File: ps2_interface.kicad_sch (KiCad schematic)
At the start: 28 parts, among them J1 Mini-DIN-6, J2 Conn_01x13, J3 KBD, U1 74HC595, U2 74HC595, U3 74HC180, U4 74HC08, U5 74HC14

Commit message: Update
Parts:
- removed TP1: REG_CLK, TestPoint:TestPoint_Loop_D2.60mm_Drill1.6mm_Beaded, symbol Connector:TestPoint
- removed TP2: LATCH_CLK, TestPoint:TestPoint_Loop_D2.60mm_Drill1.6mm_Beaded, symbol Connector:TestPoint
- removed U3: 74HC180, Package_DIP:DIP-14_W7.62mm, symbol AK's_Library:74HC180
- added U6: 74HC280, Package_DIP:DIP-14_W7.62mm, symbol 74xx:74LS280
- J2: footprint Connector_PinSocket_2.54mm:PinSocket_1x13_P2.54mm_Vertical -> Connector_PinHeader_2.54mm:PinHeader_1x13_P2.54mm_Vertical
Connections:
- net BUS_ENABLE: now also U5.3; no longer U5.11
- net D0: now also U6.1 (G)
- net D1: now also U6.13 (F)
- net D2: now also U6.8 (A)
- net D3: now also U6.9 (B)
- net D4: now also U6.10 (C)
- net D5: now also U6.11 (D)
- net D6: now also U6.4 (I)
- net D7: now also U6.12 (E)
- net DE: now also U4.12; no longer U4.1
- net DP: now also U6.2 (H); no longer U5.9
- net GND: now also U6.7 (GND)
- net KBD_CLK: now also U5.11; no longer U5.3
- net VALID_PACKET: now also U4.8; no longer U4.6
- net VCC: now also U5.9, U6.14 (VCC); no longer U4.12, U4.9
- net ~{LATCH_CLK}: now also U4.3; no longer U4.8
- net ~{REG_CLK}: now also U4.4, U4.5; no longer U4.13
- net ~{REG_OE}: now also U5.4; no longer U5.10
- net at U4.11: now also U4.9; no longer U4.10
- net at U5.2: now also U4.13; no longer U4.2
- net at D1.2 (A), R1.1: now also U5.10; no longer U5.4
- new net: U4.10, U6.6 (Odd)
- new net: U4.1, U4.2, U4.6
- no-connect marks 9 -> 10
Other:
- moved on the sheet: U4A, U4B, U4C, U4D, U5B, U5D, U5E

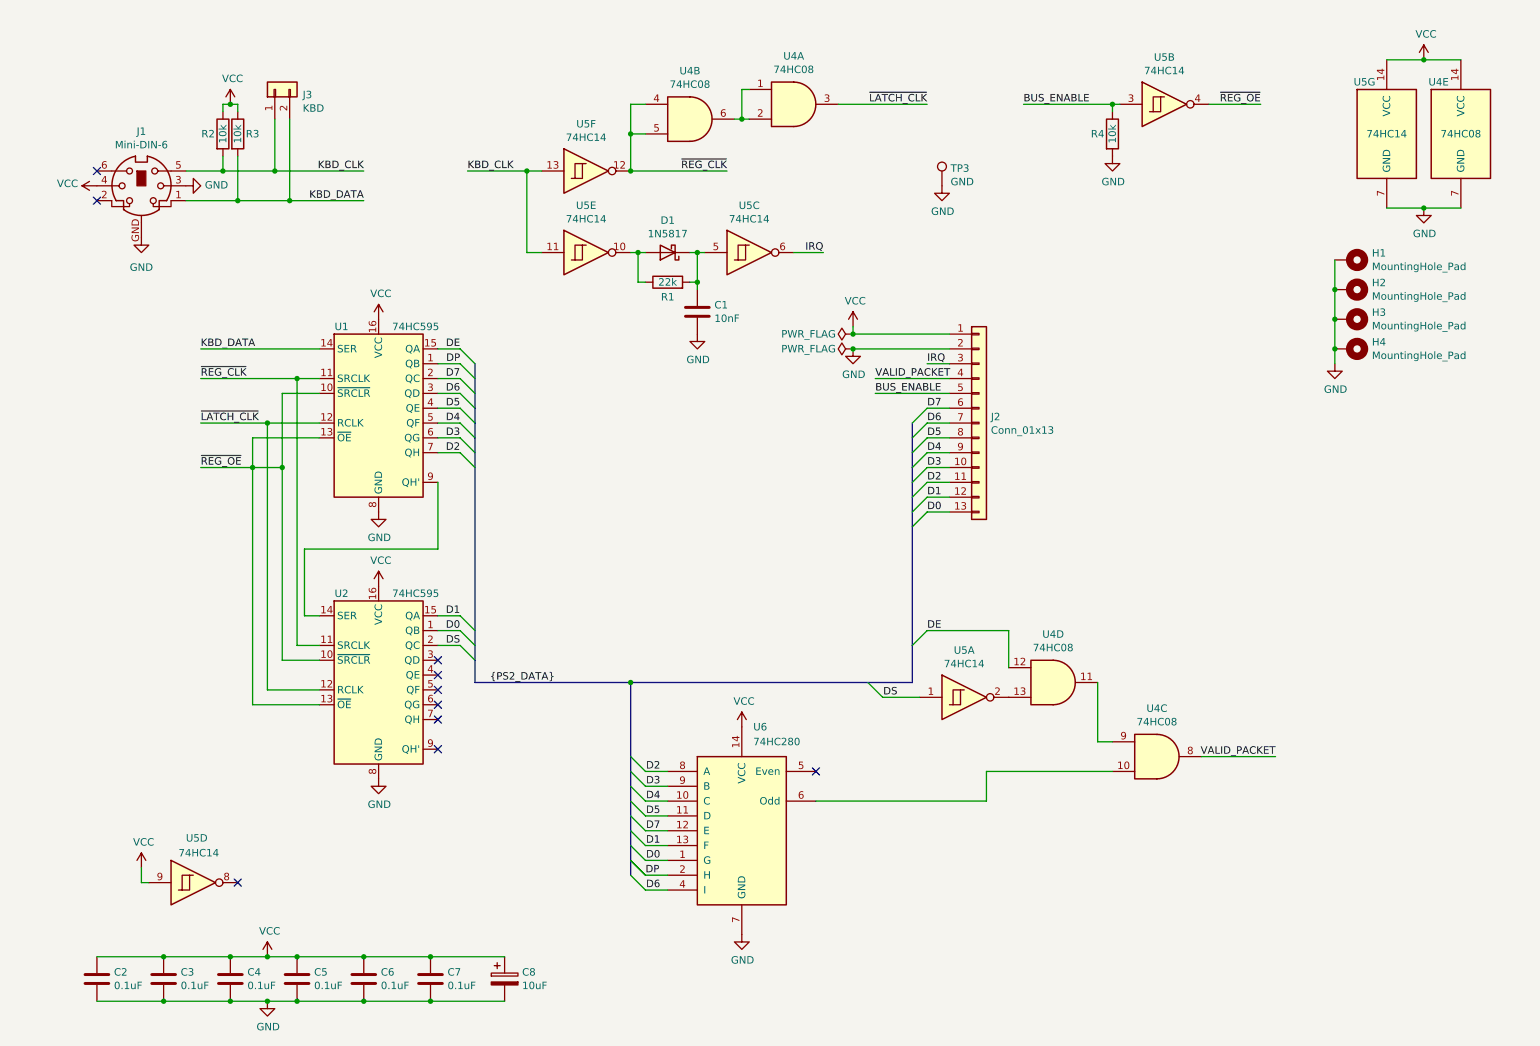
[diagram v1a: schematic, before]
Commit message: Add auto reset
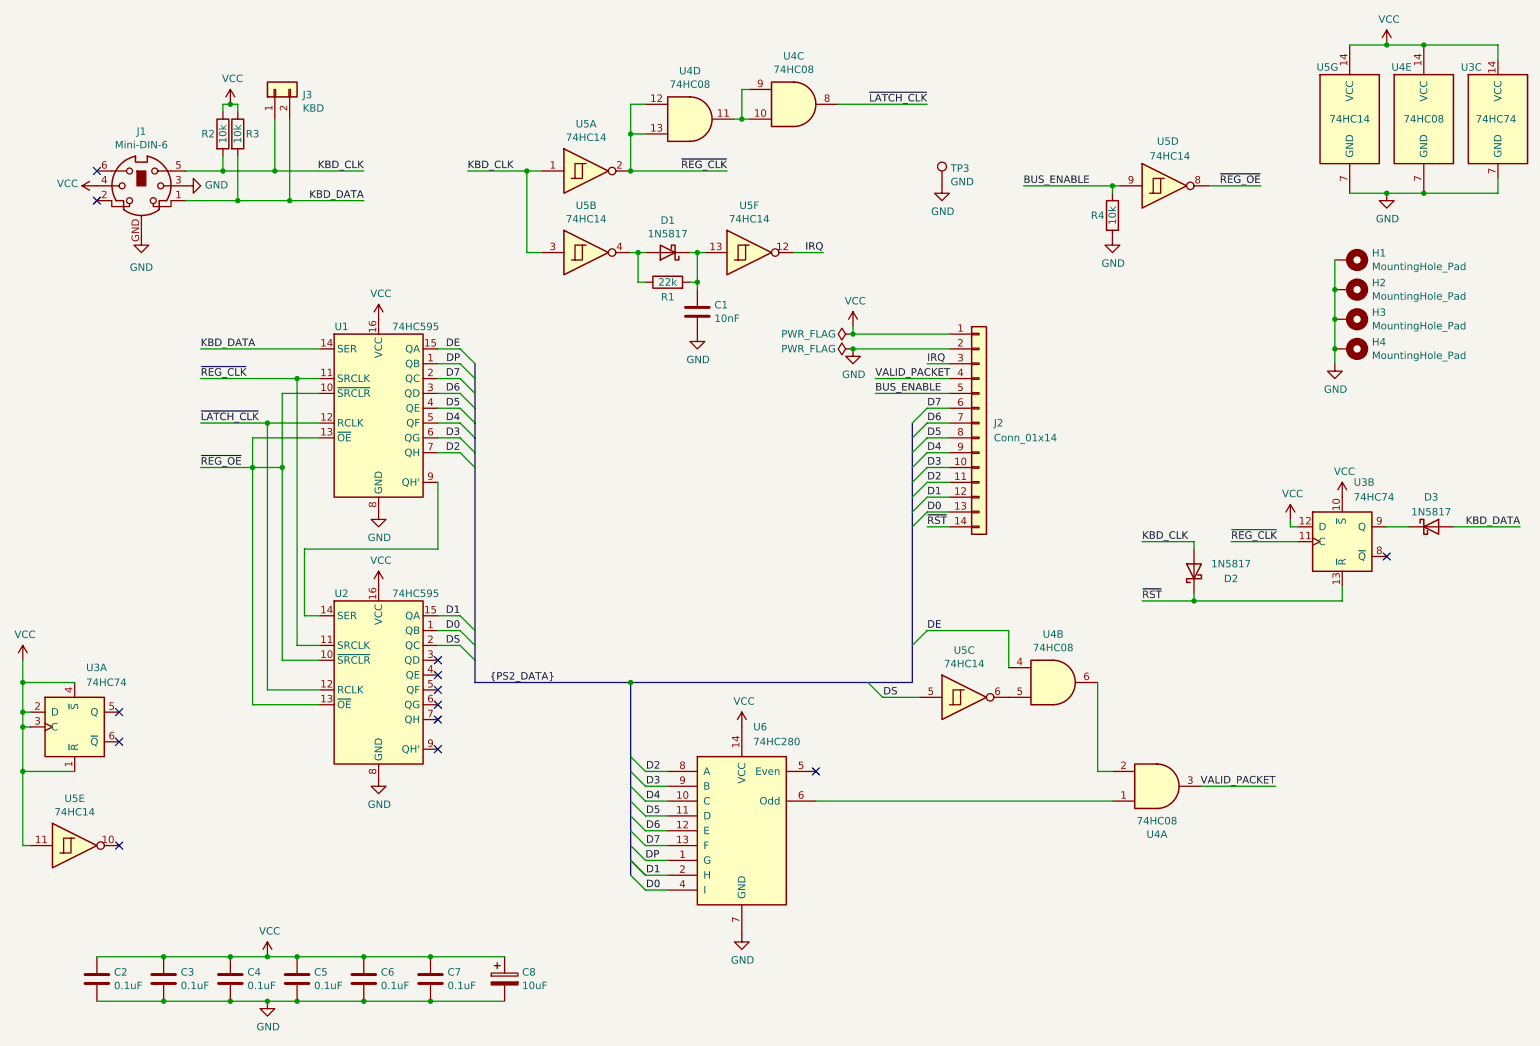
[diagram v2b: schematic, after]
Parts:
- removed J2: Conn_01x13, Connector_PinHeader_2.54mm:PinHeader_1x13_P2.54mm_Vertical, symbol Connector_Generic:Conn_01x13
- added D2, D3: 1N5817, Diode_THT:D_DO-41_SOD81_P7.62mm_Horizontal, symbol Diode:1N5817
- added J2: Conn_01x14, Connector_PinHeader_2.54mm:PinHeader_1x14_P2.54mm_Vertical, symbol Connector_Generic:Conn_01x14
- added U3: 74HC74, Package_DIP:DIP-14_W7.62mm, symbol 74xx:74LS74
- J3: footprint Connector_PinHeader_2.54mm:PinHeader_1x02_P2.54mm_Vertical -> Connector_PinSocket_2.54mm:PinSocket_1x02_P2.54mm_Vertical
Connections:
- net BUS_ENABLE: now also U5.9, J2.5 (Pin_5); no longer U5.3
- net D0: now also U6.4 (I), J2.13 (Pin_13); no longer U6.1 (G)
- net D1: now also U6.2 (H), J2.12 (Pin_12); no longer U6.13 (F)
- net D2: now also J2.11 (Pin_11)
- net D3: now also J2.10 (Pin_10)
- net D4: now also J2.9 (Pin_9)
- net D5: now also J2.8 (Pin_8)
- net D6: now also U6.12 (E), J2.7 (Pin_7); no longer U6.4 (I)
- net D7: now also U6.13 (F), J2.6 (Pin_6); no longer U6.12 (E)
- net DE: now also U4.4; no longer U4.12
- net DP: now also U6.1 (G); no longer U6.2 (H)
- net DS: now also U5.5; no longer U5.1
- net GND: now also J2.2 (Pin_2), U3.7 (GND)
- net IRQ: now also U5.12, J2.3 (Pin_3); no longer U5.6
- net KBD_CLK: now also U5.1, U5.3, D2.2 (A); no longer U5.11, U5.13
- net KBD_DATA: now also D3.2 (A)
- net VALID_PACKET: now also U4.3, J2.4 (Pin_4); no longer U4.8
- net VCC: now also U5.11, J2.1 (Pin_1), U3.1 (~{R}), U3.10 (~{S}), U3.12 (D), U3.14 (VCC), U3.2 (D), U3.3 (C), U3.4 (~{S}); no longer U5.9
- net ~{LATCH_CLK}: now also U4.8; no longer U4.3
- net ~{REG_CLK}: now also U4.12, U4.13, U5.2, U3.11 (C); no longer U4.4, U4.5, U5.12
- net ~{REG_OE}: now also U5.8; no longer U5.4
- net at U4.11, U4.9: now also U4.10
- net at U6.6 (Odd): now also U4.1; no longer U4.10
- net at D1.2 (A), R1.1: now also U5.4; no longer U5.10
- net at U4.2, U4.6: no longer U4.1
- net at C1.1, D1.1 (K), R1.2: now also U5.13; no longer U5.5
- new net: U4.5, U5.6
- new net: D3.1 (K), U3.9 (Q)
- new net ~{RST}: D2.1 (K), J2.14 (Pin_14), U3.13 (~{R})
- no-connect marks 10 -> 13
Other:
- moved on the sheet: R4, U4A, U4B, U4C, U4D, U4E, U5A, U5B, U5C, U5D, U5E, U5F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
